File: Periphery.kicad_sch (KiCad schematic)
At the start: 26 parts, among them SW1 Mitsumi R-667996, SW2 Mitsumi R-667996, U2 SN74LV595A, U3 THVD1420DRLR, U4 TPS2521ARPWR, U5 SN74LV595A, U6 TS5A3159DCK

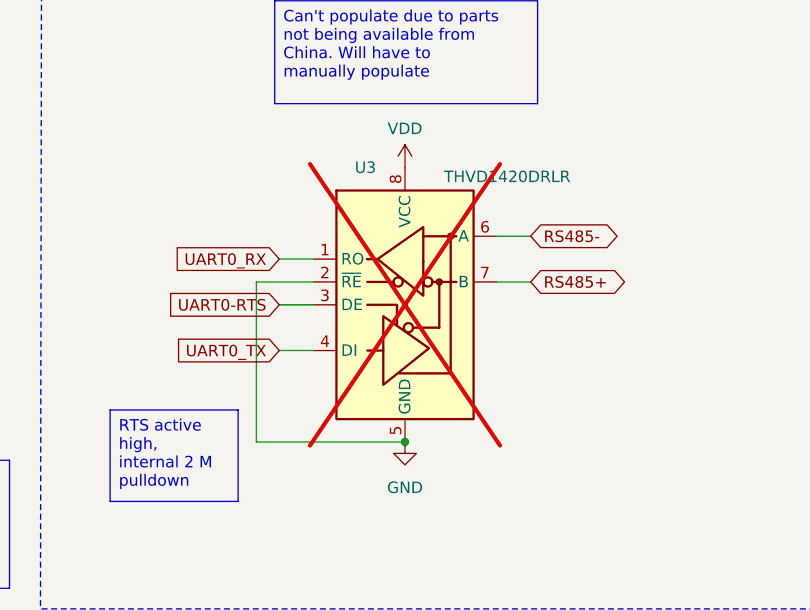
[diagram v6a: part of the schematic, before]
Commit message: Fixed BOM LCSC part numbers mostly
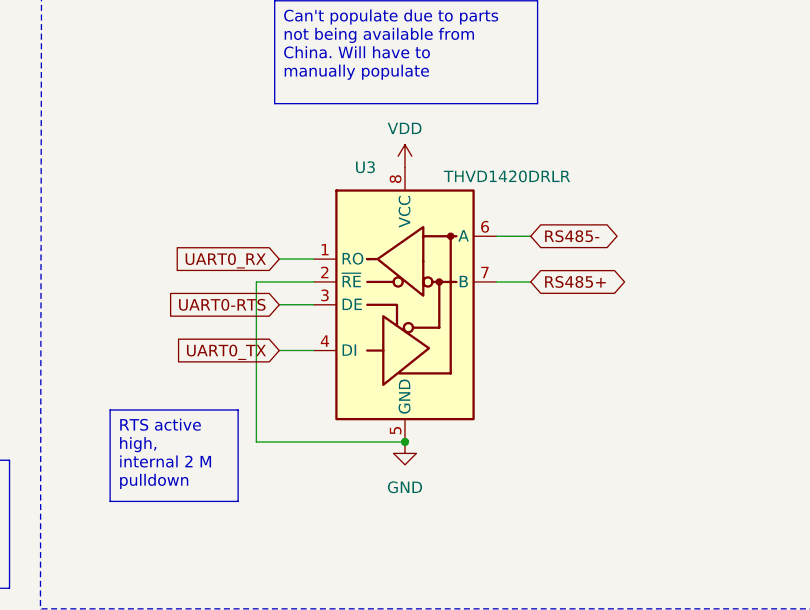
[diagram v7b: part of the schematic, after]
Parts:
- C17: LCSC C52923 -> C272874
- C18: LCSC C52923 -> C541392
- C19, C20, C21, C22: LCSC C52923 -> C318576
- R11: LCSC C25744 -> C25790
- R12: LCSC C25744 -> C138005
- R14: LCSC C25744 -> C25741
- R15: LCSC C25744 -> C321224
- R16: LCSC C25744 -> C25079
- R21: LCSC C25744 -> C25755
- U2, U5: LCSC (none) -> C6297201
- U3: LCSC (none) -> C3235555; now fitted
- U4: LCSC (none) -> C3662707
- U6: LCSC (none) -> C46388
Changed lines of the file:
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@@
 			)
 		)
-		(property "LCSC" "C52923"
+		(property "LCSC" "C318576"
 			(at 39.878 148.082 0)
 			(effects
@@
 		(in_bom yes)
 		(on_board yes)
-		(dnp yes)
+		(dnp no)
 		(property "Reference" "U3"
 			(at 141.732 67.31 0)
@@
 			)
 		)
+		(property "LCSC" "C3235555"
+			(at 147.32 82.55 0)
+			(effects
+				(font
+					(size 1.27 1.27)
+				)
+				(hide yes)
+			)
+		)
 		(pin "3"
 		)
@@
 			)
 		)
-		(property "LCSC" "C52923"
+		(property "LCSC" "C318576"
 			(at 39.878 99.822 0)
 			(effects
@@
 			)
 		)
-		(property "LCSC" "C25744"
+		(property "LCSC" "C25741"
 			(at 178.054 141.986 0)
 			(effects
@@
 			)
 		)
-		(property "LCSC" "C52923"
+		(property "LCSC" "C541392"
 			(at 146.558 158.242 0)
 			(effects
@@
 			)
 		)
-		(property "LCSC" "C52923"
+		(property "LCSC" "C318576"
 			(at 29.718 99.822 0)
 			(effects
@@
 			)
 		)
-		(property "LCSC" "C52923"
+		(property "LCSC" "C272874"
 			(at 159.258 158.242 0)
 			(effects
@@
 			)
 		)
-		(property "LCSC" "C52923"
+		(property "LCSC" "C318576"
 			(at 29.718 148.082 0)
 			(effects
@@
 			)
 		)
-		(property "LCSC" "C25744"
+		(property "LCSC" "C321224"
 			(at 169.164 147.066 0)
 			(effects
@@
 			)
 		)
+		(property "LCSC" "C6297201"
+			(at 54.61 134.62 0)
+			(effects
+				(font
+					(size 1.27 1.27)
+				)
+				(hide yes)
+			)
+		)
 		(pin "2"
 		)
@@
 			)
 		)
+		(property "LCSC" "C46388"
+			(at 233.68 74.93 0)
+			(effects
+				(font
+					(size 1.27 1.27)
+				)
+				(hide yes)
+			)
+		)
 		(pin "5"
 		)
@@
 			)
 		)
+		(property "LCSC" "C46388"
+			(at 261.62 74.93 0)
+			(effects
+				(font
+					(size 1.27 1.27)
+				)
+				(hide yes)
+			)
+		)
 		(pin "5"
 		)
@@
 			)
 		)
+		(property "LCSC" "C6297201"
+			(at 54.61 87.63 0)
+			(effects
+				(font
+					(size 1.27 1.27)
+				)
+				(hide yes)
+			)
+		)
 		(pin "2"
 		)
@@
 			)
 		)
-		(property "LCSC" "C25744"
+		(property "LCSC" "C25790"
 			(at 133.604 131.826 0)
 			(effects
@@
 			)
 		)
+		(property "LCSC" "C3662707"
+			(at 151.13 142.24 0)
+			(effects
+				(font
+					(size 1.27 1.27)
+				)
+				(hide yes)
+			)
+		)
 		(pin "1"
 		)
@@
 			)
 		)
-		(property "LCSC" "C25744"
+		(property "LCSC" "C25755"
 			(at 178.054 133.096 0)
 			(effects
@@
 			)
 		)
-		(property "LCSC" "C25744"
+		(property "LCSC" "C138005"
 			(at 133.604 138.176 0)
 			(effects
@@
 			)
 		)
-		(property "LCSC" "C25744"
+		(property "LCSC" "C25079"
 			(at 224.028 79.756 0)
 			(effects

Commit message: Found substitute part
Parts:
- U2, U5: LCSC C6297201 -> C7083313
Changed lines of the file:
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@@
 			)
 		)
-		(property "LCSC" "C6297201"
+		(property "LCSC" "C7083313"
 			(at 54.61 134.62 0)
 			(effects
@@
 			)
 		)
-		(property "LCSC" "C6297201"
+		(property "LCSC" "C7083313"
 			(at 54.61 87.63 0)
 			(effects
